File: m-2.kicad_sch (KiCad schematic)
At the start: 14 parts, among them J3 Bus_M.2_1-2199230-6, Y1 Oscillator_SMD_32.768kHz_ECS_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

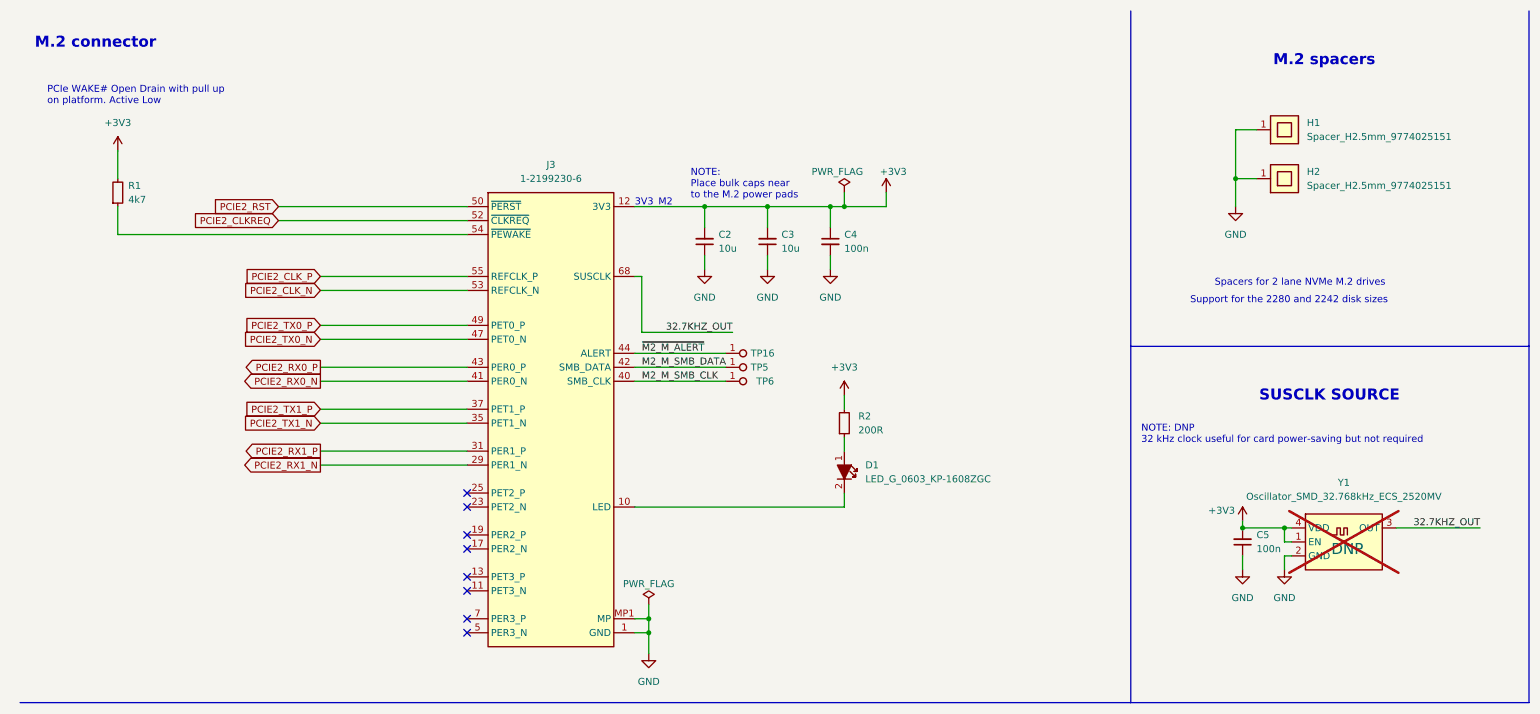
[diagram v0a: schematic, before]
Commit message: Updated symbols from lib. Minor DRC and ERC fixes
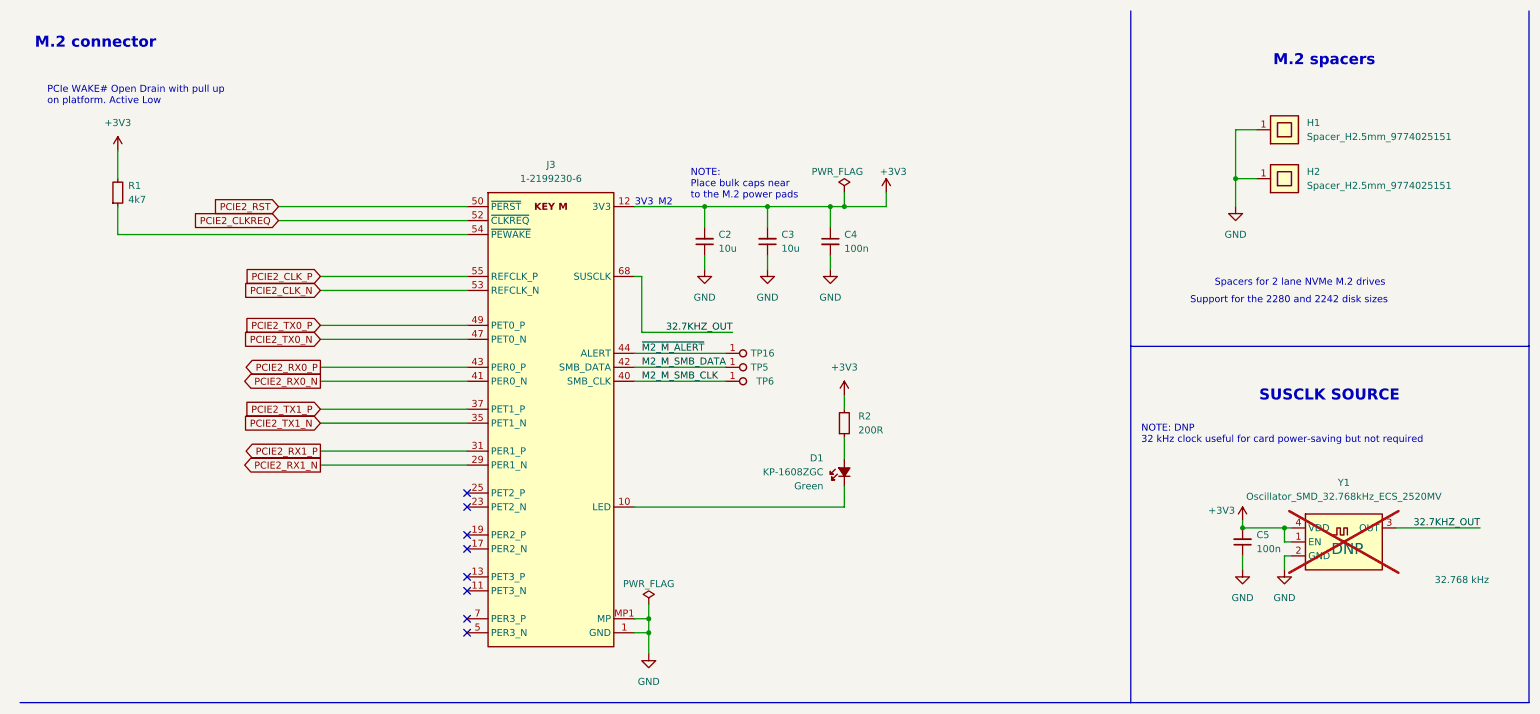
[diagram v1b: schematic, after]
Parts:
- D1: Color (none) -> Green
- Y1: Manufacturer ECS Inc. -> ECS Inc. International; Val (none) -> 32.768 kHz
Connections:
- net at R2.1: now also D1.2 (A); no longer D1.1
- net at J3.10 (LED): now also D1.1 (C); no longer D1.2
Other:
- moved on the sheet: D1
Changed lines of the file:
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@@
     (stroke (width 0) (type default))
   )
-  (wire (pts (xy 162.56 100.33) (xy 162.56 102.87))
+  (wire (pts (xy 162.56 99.06) (xy 162.56 102.87))
     (stroke (width 0) (type default))
   )
@@
     (stroke (width 0) (type default))
   )
-  (wire (pts (xy 162.56 90.17) (xy 162.56 92.71))
+  (wire (pts (xy 162.56 90.17) (xy 162.56 93.98))
     (stroke (width 0) (type default))
   )
@@
       (effects (font (size 1.27 1.27)) hide)
     )
+    (property "Author" "Antmicro" (at 146.05 67.31 0)
+      (effects (font (size 1.27 1.27) (thickness 0.15)) (justify left bottom) hide)
+    )
+    (property "License" "Apache-2.0" (at 146.05 69.85 0)
+      (effects (font (size 1.27 1.27) (thickness 0.15)) (justify left bottom) hide)
+    )
     (pin "1")
     (instances
@@
       (effects (font (size 1.27 1.27)) hide)
     )
+    (property "Author" "Antmicro" (at 185.42 48.26 0)
+      (effects (font (size 1.27 1.27) (thickness 0.15)) (justify left bottom) hide)
+    )
+    (property "License" "Apache-2.0" (at 185.42 50.8 0)
+      (effects (font (size 1.27 1.27) (thickness 0.15)) (justify left bottom) hide)
+    )
     (pin "1")
     (instances
@@
       (effects (font (size 1.27 1.27) (thickness 0.15)) (justify left bottom) hide)
     )
-    (property "Datasheet" "https://www.we-online.com/components/products/datasheet/9774025151.pdf" (at 260.35 44.45 0)
+    (property "Datasheet" "https://www.we-online.com/components/products/datasheet/9774025151R.pdf" (at 260.35 44.45 0)
       (effects (font (size 1.27 1.27) (thickness 0.15)) (justify left bottom) hide)
     )
@@
       (effects (font (size 1.27 1.27)) hide)
     )
+    (property "Author" "Antmicro" (at 168.91 67.31 0)
+      (effects (font (size 1.27 1.27) (thickness 0.15)) (justify left bottom) hide)
+    )
+    (property "License" "Apache-2.0" (at 168.91 69.85 0)
+      (effects (font (size 1.27 1.27) (thickness 0.15)) (justify left bottom) hide)
+    )
     (pin "1")
     (instances
@@
       (effects (font (size 1.27 1.27) (thickness 0.15)) (justify left bottom) hide)
     )
-    (property "Datasheet" "https://search.murata.co.jp/Ceramy/image/img/A01X/G101/ENG/GRM155R61H104KE14-01.pdf" (at 250.19 91.44 0)
+    (property "Datasheet" "https://www.murata.com/products/productdetail?partno=GRM155R61H104KE14%23" (at 250.19 91.44 0)
       (effects (font (size 1.27 1.27) (thickness 0.15)) (justify left bottom) hide)
     )
@@
       (effects (font (size 1.27 1.27)) hide)
     )
+    (property "Author" "Antmicro" (at 243.84 121.92 0)
+      (effects (font (size 1.27 1.27) (thickness 0.15)) (justify left bottom) hide)
+    )
+    (property "License" "Apache-2.0" (at 243.84 124.46 0)
+      (effects (font (size 1.27 1.27) (thickness 0.15)) (justify left bottom) hide)
+    )
     (pin "1")
     (instances
@@
       (effects (font (size 1.27 1.27) (thickness 0.15)) (justify left bottom) hide)
     )
-    (property "Datasheet" "https://eu.mouser.com/datasheet/2/122/ECS_327MVATX-2580060.pdf" (at 295.91 118.11 0)
+    (property "Datasheet" "https://ecsxtal.com/store/pdf/ECS-327MVATX.pdf" (at 295.91 118.11 0)
       (effects (font (size 1.27 1.27) (thickness 0.15)) (justify left bottom) hide)
     )
@@
       (effects (font (size 1.27 1.27) (thickness 0.15)) (justify left bottom) hide)
     )
-    (property "Manufacturer" "ECS Inc." (at 295.91 123.19 0)
+    (property "Manufacturer" "ECS Inc. International" (at 295.91 123.19 0)
       (effects (font (size 1.27 1.27) (thickness 0.15)) (justify left bottom) hide)
     )
@@
       (effects (font (size 2 2)))
     )
+    (property "Val" "32.768 kHz" (at 269.875 116.84 0)
+      (effects (font (size 1.27 1.27) (thickness 0.15)) (justify left bottom))
+    )
     (pin "1")
     (pin "2")
@@
       (effects (font (size 1.27 1.27)) hide)
     )
+    (property "Author" "Antmicro" (at 242.57 55.88 0)
+      (effects (font (size 1.27 1.27) (thickness 0.15)) (justify left bottom) hide)
+    )
+    (property "License" "Apache-2.0" (at 242.57 58.42 0)
+      (effects (font (size 1.27 1.27) (thickness 0.15)) (justify left bottom) hide)
+    )
     (pin "1")
     (instances
@@
     )
   )
-  (symbol (lib_id "antmicroLEDIndicationDiscrete:LED_G_0603_KP-1608ZGC") (at 162.56 92.71 270) (unit 1)
+  (symbol (lib_id "antmicroLEDIndicationDiscrete:LED_G_0603_KP-1608ZGC") (at 162.56 99.06 90) (unit 1)
     (in_bom yes) (on_board yes) (dnp no) (fields_autoplaced)
-    (property "Reference" "D1" (at 166.37 95.2499 90)
+    (property "Reference" "D1" (at 158.75 93.98 90)
       (effects (font (size 1.27 1.27) (thickness 0.15)) (justify left))
     )
-    (property "Value" "LED_G_0603_KP-1608ZGC" (at 166.37 97.7899 90)
-      (effects (font (size 1.27 1.27) (thickness 0.15)) (justify left))
+    (property "Value" "LED_G_0603_KP-1608ZGC" (at 165.1 96.52 90)
+      (effects (font (size 1.27 1.27) (thickness 0.15)) (justify right) hide)
     )
-    (property "Footprint" "antmicro-footprints:LED_0603_1608Metric_G" (at 152.4 115.57 0)
+    (property "Footprint" "antmicro-footprints:LED_0603_1608Metric_G" (at 172.72 76.2 0)
       (effects (font (size 1.27 1.27) (thickness 0.15)) (justify left bottom) hide)
     )
-    (property "Datasheet" "https://www.farnell.com/datasheets/2045914.pdf" (at 149.86 115.57 0)
+    (property "Datasheet" "https://www.kingbright.com/attachments/file/psearch/000/00/00/KP-1608ZGC(Ver.19B).pdf" (at 175.26 76.2 0)
       (effects (font (size 1.27 1.27) (thickness 0.15)) (justify left bottom) hide)
     )
-    (property "MPN" "KP-1608ZGC" (at 147.32 115.57 0)
-      (effects (font (size 1.27 1.27) (thickness 0.15)) (justify left bottom) hide)
+    (property "MPN" "KP-1608ZGC" (at 158.75 96.52 90)
+      (effects (font (size 1.27 1.27) (thickness 0.15)) (justify left))
     )
-    (property "Manufacturer" "Kingbright" (at 144.78 115.57 0)
+    (property "Manufacturer" "Kingbright" (at 180.34 76.2 0)
       (effects (font (size 1.27 1.27) (thickness 0.15)) (justify left bottom) hide)
     )
-    (property "Author" "Antmicro" (at 142.24 115.57 0)
+    (property "Author" "Antmicro" (at 182.88 76.2 0)
       (effects (font (size 1.27 1.27) (thickness 0.15)) (justify left bottom) hide)
     )
-    (property "License" "Apache-2.0" (at 139.7 115.57 0)
+    (property "License" "Apache-2.0" (at 185.42 76.2 0)
       (effects (font (size 1.27 1.27) (thickness 0.15)) (justify left bottom) hide)
     )
+    (property "Color" "Green" (at 158.75 99.06 90)
+      (effects (font (size 1.27 1.27)) (justify left))
+    )
     (pin "1")
     (pin "2")
@@
       (effects (font (size 1.27 1.27)) hide)
     )
+    (property "Author" "Antmicro" (at 177.8 85.09 0)
+      (effects (font (size 1.27 1.27) (thickness 0.15)) (justify left bottom) hide)
+    )
+    (property "License" "Apache-2.0" (at 177.8 87.63 0)
+      (effects (font (size 1.27 1.27) (thickness 0.15)) (justify left bottom) hide)
+    )
     (pin "1")
     (instances
@@
       (effects (font (size 1.27 1.27)) hide)
     )
+    (property "Author" "Antmicro" (at 251.46 121.92 0)
+      (effects (font (size 1.27 1.27) (thickness 0.15)) (justify left bottom) hide)
+    )
+    (property "License" "Apache-2.0" (at 251.46 124.46 0)
+      (effects (font (size 1.27 1.27) (thickness 0.15)) (justify left bottom) hide)
+    )
     (pin "1")
     (instances
@@
       (effects (font (size 1.27 1.27)) hide)
     )
+    (property "Author" "Antmicro" (at 250.19 107.95 0)
+      (effects (font (size 1.27 1.27) (thickness 0.15)) (justify left bottom) hide)
+    )
+    (property "License" "Apache-2.0" (at 250.19 110.49 0)
+      (effects (font (size 1.27 1.27) (thickness 0.15)) (justify left bottom) hide)
+    )
     (pin "1")
     (instances
@@
       (effects (font (size 1.27 1.27) (thickness 0.15)) (justify left bottom) hide)
     )
-    (property "Datasheet" "https://www.we-online.com/components/products/datasheet/9774025151.pdf" (at 260.35 53.34 0)
+    (property "Datasheet" "https://www.we-online.com/components/products/datasheet/9774025151R.pdf" (at 260.35 53.34 0)
       (effects (font (size 1.27 1.27) (thickness 0.15)) (justify left bottom) hide)
     )
@@
     )
   )
-  (symbol (lib_name "Bus_M.2_1-2199230-6_1") (lib_id "antmicroPciConnectors:Bus_M.2_1-2199230-6") (at 93.98 48.26 0) (unit 1)
+  (symbol (lib_id "antmicroPciConnectors:Bus_M.2_1-2199230-6") (at 93.98 48.26 0) (unit 1)
     (in_bom yes) (on_board yes) (dnp no) (fields_autoplaced)
     (property "Reference" "J3" (at 109.22 40.64 0)
@@
       (effects (font (size 1.27 1.27)) hide)
     )
+    (property "Author" "Antmicro" (at 45.72 40.64 0)
+      (effects (font (size 1.27 1.27) (thickness 0.15)) (justify left bottom) hide)
+    )
+    (property "License" "Apache-2.0" (at 45.72 43.18 0)
+      (effects (font (size 1.27 1.27) (thickness 0.15)) (justify left bottom) hide)
+    )
     (pin "1")
     (instances
@@
       (effects (font (size 1.27 1.27)) hide)
     )
+    (property "Author" "Antmicro" (at 135.89 137.16 0)
+      (effects (font (size 1.27 1.27) (thickness 0.15)) (justify left bottom) hide)
+    )
+    (property "License" "Apache-2.0" (at 135.89 139.7 0)
+      (effects (font (size 1.27 1.27) (thickness 0.15)) (justify left bottom) hide)
+    )
     (pin "1")
     (instances
@@
       (effects (font (size 1.27 1.27)) hide)
     )
+    (property "Author" "Antmicro" (at 157.48 67.31 0)
+      (effects (font (size 1.27 1.27) (thickness 0.15)) (justify left bottom) hide)
+    )
+    (property "License" "Apache-2.0" (at 157.48 69.85 0)
+      (effects (font (size 1.27 1.27) (thickness 0.15)) (justify left bottom) hide)
+    )
     (pin "1")

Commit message: [#83351] Project refresh 81589
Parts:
- Y1: DNP DNP -> (none)
